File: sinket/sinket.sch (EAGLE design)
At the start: 20 parts, among them IC1 ATTINY85-20PU, IC2 TS2940CP50S

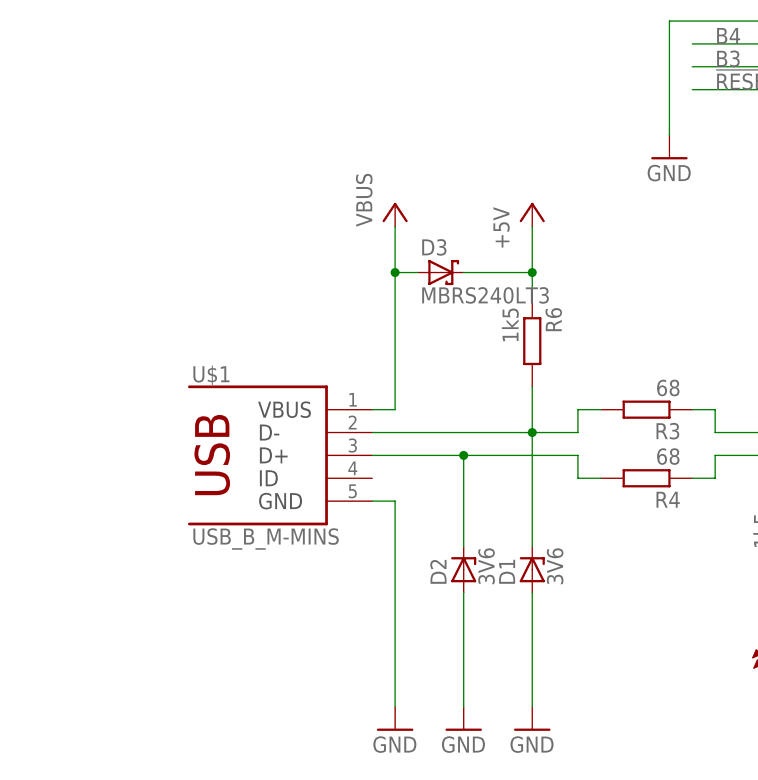
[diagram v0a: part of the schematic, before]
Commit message: sinket: add fuse
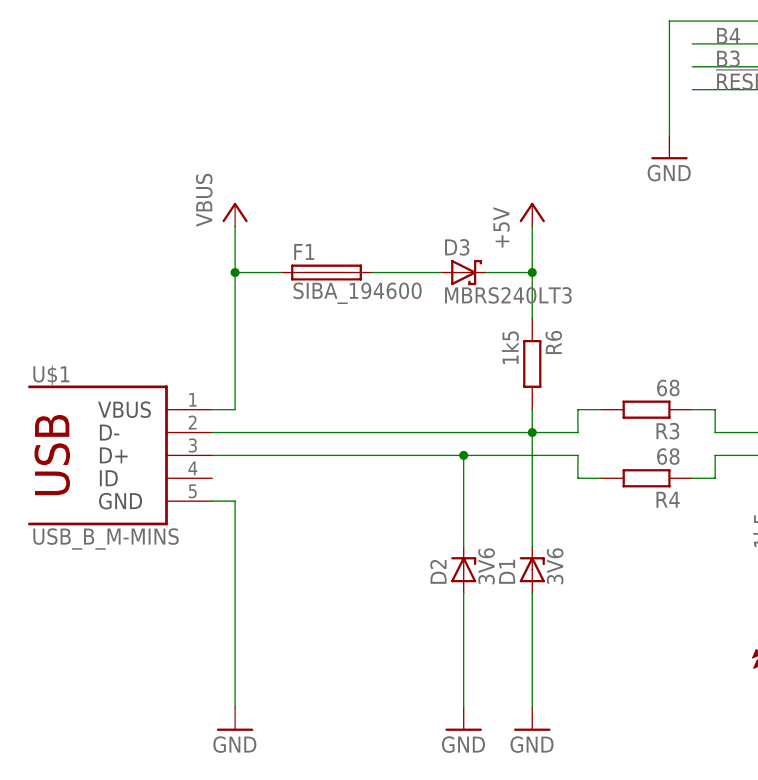
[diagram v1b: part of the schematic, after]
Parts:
- added F1: SIBA_194600, n39:SIBA_194600
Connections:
- new net N$2: D3.A, F1.2
- net VBUS: now also F1.1; no longer D3.A
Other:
- moved on the sheet: D3, R6, U$1
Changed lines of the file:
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@@
 <part name="GND10" library="supply1" deviceset="GND" device=""/>
 <part name="GND11" library="supply1" deviceset="GND" device=""/>
+<part name="F1" library="n39" deviceset="SIBA_194600" device=""/>
 </parts>
 <sheets>
@@
 </plain>
 <instances>
-<instance part="U$1" gate="G$1" x="5.08" y="53.34"/>
-<instance part="P+1" gate="VCC" x="20.32" y="81.28"/>
-<instance part="GND1" gate="1" x="20.32" y="22.86"/>
+<instance part="U$1" gate="G$1" x="-12.7" y="53.34"/>
+<instance part="P+1" gate="VCC" x="2.54" y="81.28"/>
+<instance part="GND1" gate="1" x="2.54" y="22.86"/>
 <instance part="P+2" gate="VCC" x="129.54" y="93.98"/>
 <instance part="P+3" gate="1" x="160.02" y="93.98"/>
@@
 <instance part="R4" gate="G$1" x="48.26" y="50.8" rot="R180"/>
 <instance part="R5" gate="G$1" x="177.8" y="53.34" rot="R270"/>
-<instance part="R6" gate="G$1" x="35.56" y="66.04" rot="R270"/>
+<instance part="R6" gate="G$1" x="35.56" y="63.5" rot="R270"/>
 <instance part="P+7" gate="1" x="35.56" y="81.28"/>
 <instance part="D1" gate="G$1" x="35.56" y="40.64" rot="R90"/>
@@
 <instance part="C1" gate="G$1" x="165.1" y="53.34"/>
 <instance part="GND8" gate="1" x="177.8" y="22.86"/>
-<instance part="D3" gate="G$1" x="25.4" y="73.66"/>
+<instance part="D3" gate="G$1" x="27.94" y="73.66"/>
 <instance part="IC2" gate="IC$1" x="139.7" y="86.36"/>
 <instance part="C2" gate="G$1" x="129.54" y="81.28"/>
@@
 <instance part="GND10" gate="1" x="149.86" y="71.12"/>
 <instance part="GND11" gate="1" x="139.7" y="71.12"/>
+<instance part="F1" gate="G$1" x="12.7" y="73.66"/>
 </instances>
 <busses>
@@
 <wire x1="35.56" y1="78.74" x2="35.56" y2="73.66" width="0.1524" layer="91"/>
 <pinref part="D3" gate="G$1" pin="C"/>
-<wire x1="35.56" y1="73.66" x2="35.56" y2="71.12" width="0.1524" layer="91"/>
-<wire x1="27.94" y1="73.66" x2="35.56" y2="73.66" width="0.1524" layer="91"/>
+<wire x1="35.56" y1="73.66" x2="35.56" y2="68.58" width="0.1524" layer="91"/>
+<wire x1="30.48" y1="73.66" x2="35.56" y2="73.66" width="0.1524" layer="91"/>
 <junction x="35.56" y="73.66"/>
 </segment>
@@
 <segment>
 <pinref part="P+1" gate="VCC" pin="VCC"/>
-<wire x1="20.32" y1="78.74" x2="20.32" y2="73.66" width="0.1524" layer="91"/>
 <pinref part="U$1" gate="G$1" pin="1"/>
-<wire x1="20.32" y1="73.66" x2="20.32" y2="58.42" width="0.1524" layer="91"/>
-<wire x1="20.32" y1="58.42" x2="17.78" y2="58.42" width="0.1524" layer="91"/>
-<pinref part="D3" gate="G$1" pin="A"/>
-<wire x1="20.32" y1="73.66" x2="22.86" y2="73.66" width="0.1524" layer="91"/>
-<junction x="20.32" y="73.66"/>
+<wire x1="2.54" y1="78.74" x2="2.54" y2="73.66" width="0.1524" layer="91"/>
+<wire x1="2.54" y1="73.66" x2="2.54" y2="58.42" width="0.1524" layer="91"/>
+<wire x1="2.54" y1="58.42" x2="0" y2="58.42" width="0.1524" layer="91"/>
+<pinref part="F1" gate="G$1" pin="1"/>
+<wire x1="7.62" y1="73.66" x2="2.54" y2="73.66" width="0.1524" layer="91"/>
+<junction x="2.54" y="73.66"/>
 </segment>
 <segment>
@@
 <pinref part="U$1" gate="G$1" pin="5"/>
 <pinref part="GND1" gate="1" pin="GND"/>
-<wire x1="17.78" y1="48.26" x2="20.32" y2="48.26" width="0.1524" layer="91"/>
-<wire x1="20.32" y1="48.26" x2="20.32" y2="25.4" width="0.1524" layer="91"/>
+<wire x1="0" y1="48.26" x2="2.54" y2="48.26" width="0.1524" layer="91"/>
+<wire x1="2.54" y1="48.26" x2="2.54" y2="25.4" width="0.1524" layer="91"/>
 </segment>
 <segment>
@@
 <pinref part="U$1" gate="G$1" pin="2"/>
 <pinref part="R3" gate="G$1" pin="2"/>
-<wire x1="17.78" y1="55.88" x2="35.56" y2="55.88" width="0.1524" layer="91"/>
+<wire x1="0" y1="55.88" x2="35.56" y2="55.88" width="0.1524" layer="91"/>
 <wire x1="35.56" y1="55.88" x2="40.64" y2="55.88" width="0.1524" layer="91"/>
 <wire x1="40.64" y1="55.88" x2="40.64" y2="58.42" width="0.1524" layer="91"/>
 <wire x1="40.64" y1="58.42" x2="43.18" y2="58.42" width="0.1524" layer="91"/>
 <pinref part="R6" gate="G$1" pin="2"/>
-<wire x1="35.56" y1="60.96" x2="35.56" y2="55.88" width="0.1524" layer="91"/>
+<wire x1="35.56" y1="58.42" x2="35.56" y2="55.88" width="0.1524" layer="91"/>
 <junction x="35.56" y="55.88"/>
 <pinref part="D1" gate="G$1" pin="C"/>
@@
 <pinref part="U$1" gate="G$1" pin="3"/>
 <pinref part="R4" gate="G$1" pin="2"/>
-<wire x1="17.78" y1="53.34" x2="27.94" y2="53.34" width="0.1524" layer="91"/>
+<wire x1="0" y1="53.34" x2="27.94" y2="53.34" width="0.1524" layer="91"/>
 <wire x1="27.94" y1="53.34" x2="40.64" y2="53.34" width="0.1524" layer="91"/>
 <wire x1="40.64" y1="53.34" x2="40.64" y2="50.8" width="0.1524" layer="91"/>
@@
 </segment>
 </net>
+<net name="N$2" class="1">
+<segment>
+<pinref part="F1" gate="G$1" pin="2"/>
+<pinref part="D3" gate="G$1" pin="A"/>
+<wire x1="17.78" y1="73.66" x2="25.4" y2="73.66" width="0.1524" layer="91"/>
+</segment>
+</net>
 </nets>
 </sheet>
 </sheets>
+<errors>
+</errors>
 </schematic>
 </drawing>

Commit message: change fuse package
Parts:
- D3: value MBRS240LT3 -> 1N5817-B; device diode:MBRS130LT3 -> diode:1N5817-B
- F1: value SIBA_194600 -> (none); device n39:SIBA_194600 -> n39:PTC-FUSE-LP60-050
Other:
- moved on the sheet: D3, F1, JP1, JP2, R6

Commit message: replace all 0805 parts with 1206 and start routing
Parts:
- C1: device rcl:C-EUC0805 -> rcl:C-EUC1206
- R1, R2, R3, R4, R5, R6: device rcl:R-EU_R0805 -> rcl:R-EU_R1206
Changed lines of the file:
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@@
 <part name="GND3" library="supply1" deviceset="GND" device=""/>
 <part name="U$6" library="n39" deviceset="JTP-1130" device="" technology="C"/>
-<part name="R1" library="rcl" deviceset="R-EU_" device="R0805" value="10k"/>
-<part name="R2" library="rcl" deviceset="R-EU_" device="R0805" value="1k5"/>
-<part name="R3" library="rcl" deviceset="R-EU_" device="R0805" value="68"/>
-<part name="R4" library="rcl" deviceset="R-EU_" device="R0805" value="68"/>
-<part name="R5" library="rcl" deviceset="R-EU_" device="R0805" value="1k5"/>
-<part name="R6" library="rcl" deviceset="R-EU_" device="R0805" value="1k5"/>
+<part name="R1" library="rcl" deviceset="R-EU_" device="R1206" value="10k"/>
+<part name="R2" library="rcl" deviceset="R-EU_" device="R1206" value="1k5"/>
+<part name="R3" library="rcl" deviceset="R-EU_" device="R1206" value="68"/>
+<part name="R4" library="rcl" deviceset="R-EU_" device="R1206" value="68"/>
+<part name="R5" library="rcl" deviceset="R-EU_" device="R1206" value="1k5"/>
+<part name="R6" library="rcl" deviceset="R-EU_" device="R1206" value="1k5"/>
 <part name="P+7" library="supply1" deviceset="+5V" device=""/>
 <part name="D1" library="diode" deviceset="ZENER-DIODE" device="SOD80C" value="3V6"/>
@@
 <part name="LED2" library="led" deviceset="LED" device="3MM" value="green"/>
 <part name="GND7" library="supply1" deviceset="GND" device=""/>
-<part name="C1" library="rcl" deviceset="C-EU" device="C0805" value="100n"/>
+<part name="C1" library="rcl" deviceset="C-EU" device="C1206" value="100n"/>
 <part name="GND8" library="supply1" deviceset="GND" device=""/>
 <part name="D3" library="diode" deviceset="1N581*" device="" technology="7-B" value="1N5817-B"/>

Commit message: LED package changed, Schraubklemme added, parts moved
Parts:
- added U$7: RIACON_101_2, n39:RIACON_101_2
- F1: value (none) -> 500mA
- LED1, LED2: device led:LED3MM -> led:LED5MM
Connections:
- net GND: now also U$7.1
- net VBAT: now also U$7.2
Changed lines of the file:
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@@
 <grid distance="0.1" unitdist="inch" unit="inch" style="lines" multiple="1" display="no" altdistance="0.01" altunitdist="inch" altunit="inch"/>
 <layers>
-<layer number="1" name="Top" color="4" fill="1" visible="no" active="no"/>
-<layer number="16" name="Bottom" color="1" fill="1" visible="no" active="no"/>
-<layer number="17" name="Pads" color="2" fill="1" visible="no" active="no"/>
-<layer number="18" name="Vias" color="2" fill="1" visible="no" active="no"/>
-<layer number="19" name="Unrouted" color="6" fill="1" visible="no" active="no"/>
-<layer number="20" name="Dimension" color="15" fill="1" visible="no" active="no"/>
-<layer number="21" name="tPlace" color="7" fill="1" visible="no" active="no"/>
-<layer number="22" name="bPlace" color="7" fill="1" visible="no" active="no"/>
-<layer number="23" name="tOrigins" color="15" fill="1" visible="no" active="no"/>
-<layer number="24" name="bOrigins" color="15" fill="1" visible="no" active="no"/>
-<layer number="25" name="tNames" color="7" fill="1" visible="no" active="no"/>
-<layer number="26" name="bNames" color="7" fill="1" visible="no" active="no"/>
-<layer number="27" name="tValues" color="7" fill="1" visible="no" active="no"/>
-<layer number="28" name="bValues" color="7" fill="1" visible="no" active="no"/>
+<layer number="1" name="Top" color="4" fill="1" visible="yes" active="no"/>
+<layer number="16" name="Bottom" color="1" fill="1" visible="yes" active="no"/>
+<layer number="17" name="Pads" color="2" fill="1" visible="yes" active="no"/>
+<layer number="18" name="Vias" color="2" fill="1" visible="yes" active="no"/>
+<layer number="19" name="Unrouted" color="6" fill="1" visible="yes" active="no"/>
+<layer number="20" name="Dimension" color="15" fill="1" visible="yes" active="no"/>
+<layer number="21" name="tPlace" color="7" fill="1" visible="yes" active="no"/>
+<layer number="22" name="bPlace" color="7" fill="1" visible="yes" active="no"/>
+<layer number="23" name="tOrigins" color="15" fill="1" visible="yes" active="no"/>
+<layer number="24" name="bOrigins" color="15" fill="1" visible="yes" active="no"/>
+<layer number="25" name="tNames" color="7" fill="1" visible="yes" active="no"/>
+<layer number="26" name="bNames" color="7" fill="1" visible="yes" active="no"/>
+<layer number="27" name="tValues" color="7" fill="1" visible="yes" active="no"/>
+<layer number="28" name="bValues" color="7" fill="1" visible="yes" active="no"/>
 <layer number="29" name="tStop" color="7" fill="3" visible="no" active="no"/>
 <layer number="30" name="bStop" color="7" fill="6" visible="no" active="no"/>
@@
 <layer number="35" name="tGlue" color="7" fill="4" visible="no" active="no"/>
 <layer number="36" name="bGlue" color="7" fill="5" visible="no" active="no"/>
-<layer number="37" name="tTest" color="7" fill="1" visible="no" active="no"/>
-<layer number="38" name="bTest" color="7" fill="1" visible="no" active="no"/>
+<layer number="37" name="tTest" color="7" fill="1" visible="yes" active="no"/>
+<layer number="38" name="bTest" color="7" fill="1" visible="yes" active="no"/>
 <layer number="39" name="tKeepout" color="4" fill="11" visible="no" active="no"/>
 <layer number="40" name="bKeepout" color="1" fill="11" visible="no" active="no"/>
@@
 <layer number="44" name="Drills" color="7" fill="1" visible="no" active="no"/>
 <layer number="45" name="Holes" color="7" fill="1" visible="no" active="no"/>
-<layer number="46" name="Milling" color="3" fill="1" visible="no" active="no"/>
-<layer number="47" name="Measures" color="7" fill="1" visible="no" active="no"/>
-<layer number="48" name="Document" color="7" fill="1" visible="no" active="no"/>
-<layer number="49" name="Reference" color="7" fill="1" visible="no" active="no"/>
-<layer number="51" name="tDocu" color="7" fill="1" visible="no" active="no"/>
-<layer number="52" name="bDocu" color="7" fill="1" visible="no" active="no"/>
+<layer number="46" name="Milling" color="3" fill="1" visible="yes" active="no"/>
+<layer number="47" name="Measures" color="7" fill="1" visible="yes" active="no"/>
+<layer number="48" name="Document" color="7" fill="1" visible="yes" active="no"/>
+<layer number="49" name="Reference" color="7" fill="1" visible="yes" active="no"/>
+<layer number="51" name="tDocu" color="7" fill="1" visible="yes" active="no"/>
+<layer number="52" name="bDocu" color="7" fill="1" visible="yes" active="no"/>
 <layer number="91" name="Nets" color="2" fill="1" visible="yes" active="yes"/>
 <layer number="92" name="Busses" color="1" fill="1" visible="yes" active="yes"/>
@@
 <part name="P+8" library="supply1" deviceset="+5V" device=""/>
 <part name="GND6" library="supply1" deviceset="GND" device=""/>
-<part name="LED1" library="led" deviceset="LED" device="3MM" value="red"/>
-<part name="LED2" library="led" deviceset="LED" device="3MM" value="green"/>
+<part name="LED1" library="led" deviceset="LED" device="5MM" value="red"/>
+<part name="LED2" library="led" deviceset="LED" device="5MM" value="green"/>
 <part name="GND7" library="supply1" deviceset="GND" device=""/>
 <part name="C1" library="rcl" deviceset="C-EU" device="C1206" value="100n"/>
@@
 <part name="GND10" library="supply1" deviceset="GND" device=""/>
 <part name="GND11" library="supply1" deviceset="GND" device=""/>
-<part name="F1" library="n39" deviceset="PTC-FUSE" device="-LP60-050"/>
+<part name="F1" library="n39" deviceset="PTC-FUSE" device="-LP60-050" value="500mA"/>
+<part name="U$7" library="n39" deviceset="RIACON_101_2" device=""/>
+<part name="GND12" library="supply1" deviceset="GND" device=""/>
 </parts>
 <sheets>
@@
 <instance part="GND11" gate="1" x="139.7" y="71.12"/>
 <instance part="F1" gate="G$1" x="12.7" y="78.74"/>
+<instance part="U$7" gate="G$1" x="111.76" y="83.82" rot="R180"/>
+<instance part="GND12" gate="1" x="119.38" y="71.12"/>
 </instances>
 <busses>
@@
 <junction x="129.54" y="86.36"/>
 <pinref part="C2" gate="G$1" pin="1"/>
+<pinref part="U$7" gate="G$1" pin="2"/>
+<wire x1="116.84" y1="86.36" x2="129.54" y2="86.36" width="0.1524" layer="91"/>
 </segment>
 <segment>
@@
 <wire x1="139.7" y1="78.74" x2="139.7" y2="73.66" width="0.1524" layer="91"/>
 </segment>
+<segment>
+<pinref part="U$7" gate="G$1" pin="1"/>
+<pinref part="GND12" gate="1" pin="GND"/>
+<wire x1="116.84" y1="83.82" x2="119.38" y2="83.82" width="0.1524" layer="91"/>
+<wire x1="119.38" y1="83.82" x2="119.38" y2="73.66" width="0.1524" layer="91"/>
+</segment>
 </net>
